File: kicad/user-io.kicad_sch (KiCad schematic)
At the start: 45 parts, among them J1 Lower Bank, J2 Upper Bank, SW1 PTS815, U1 MIMXRT1171DVMAB, U2 MAYA-W166-00B, U3 LSM6DSV, U4 LIS2MDL, U5 RTMC-G2-4IQ48, Y1 8MHz

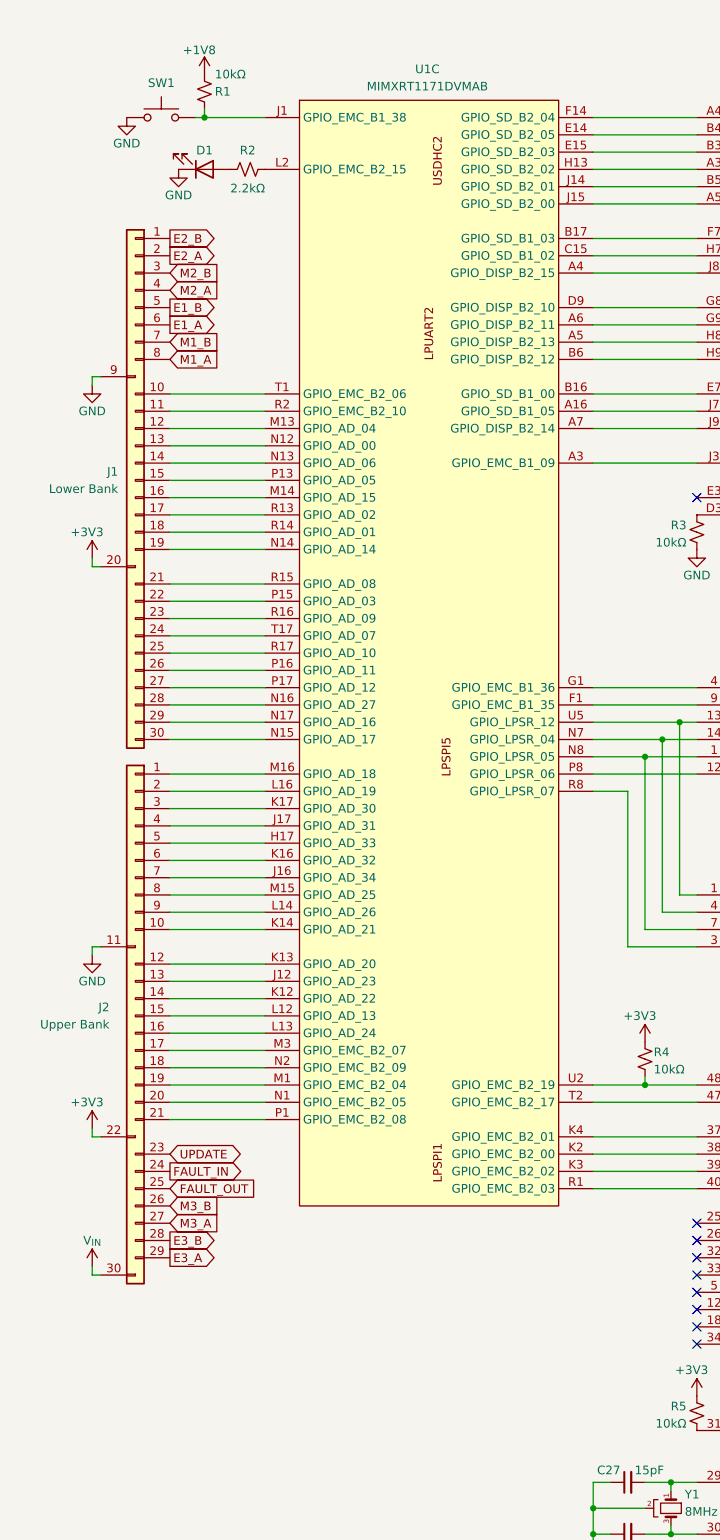
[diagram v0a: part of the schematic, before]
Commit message: moved wifi module from uSDHC2 to uSDHC1
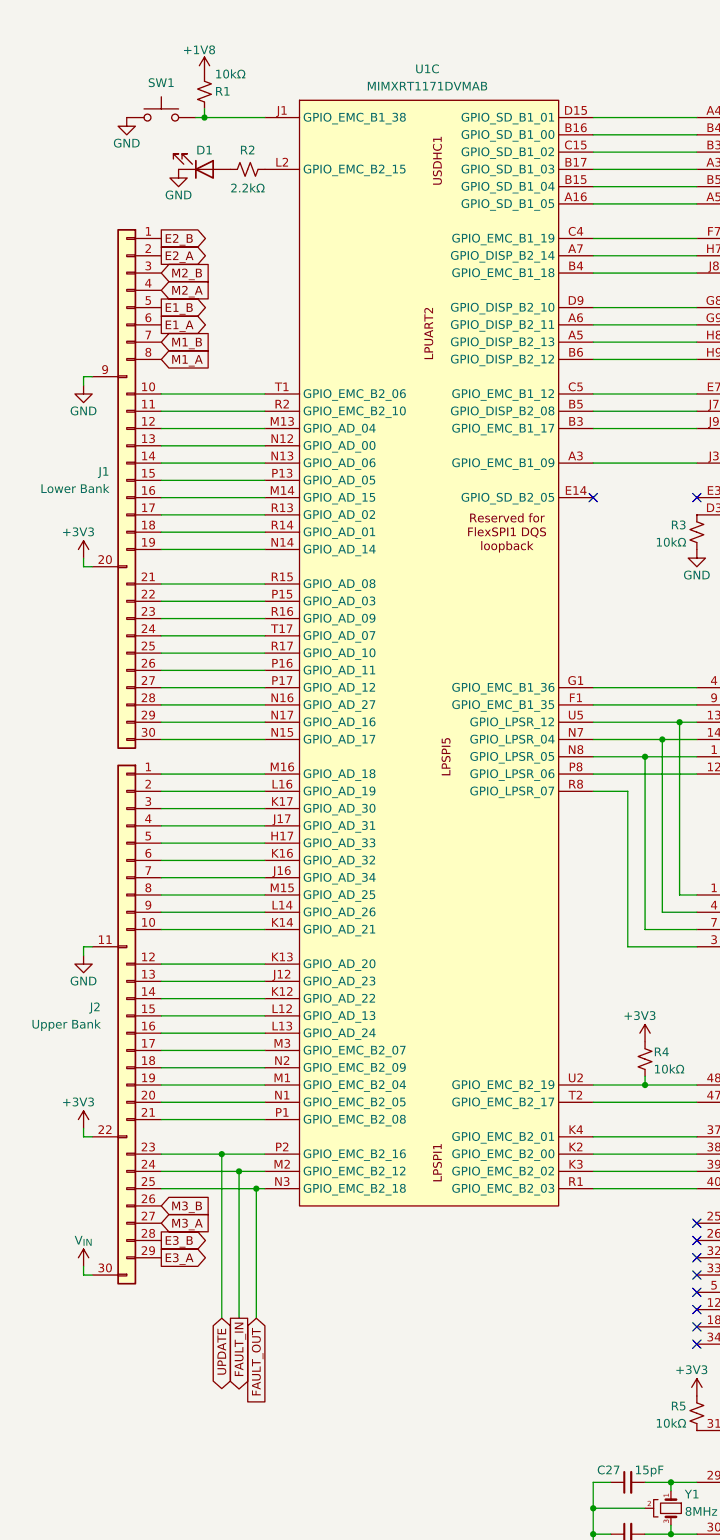
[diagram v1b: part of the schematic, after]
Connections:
- net FAULT_IN: now also U1.M2 (GPIO_EMC_B2_12)
- net FAULT_OUT: now also U1.N3 (GPIO_EMC_B2_18)
- net UPDATE: now also U1.P2 (GPIO_EMC_B2_16)
- net at U1.A16 (GPIO_SD_B1_05): now also U2.A5 (SD_DAT[3]); no longer U2.J7 (BT_RESET)
- net at U2.J8 (WLAN_DEV_WAKE): now also U1.B4 (GPIO_EMC_B1_18); no longer U1.A4 (GPIO_DISP_B2_15)
- net at U1.A7 (GPIO_DISP_B2_14): now also U2.H7 (WLAN_RESET); no longer U2.J9 (BT_DEV_WAKE)
- net at U1.B16 (GPIO_SD_B1_00): now also U2.B4 (SD_CMD); no longer U2.E7 (BT_WAKE_HOST)
- net at U1.B17 (GPIO_SD_B1_03): now also U2.A3 (SD_DAT[1]); no longer U2.F7 (WLAN_WAKE_HOST)
- net at U1.C15 (GPIO_SD_B1_02): now also U2.B3 (SD_DAT[0]); no longer U2.H7 (WLAN_RESET)
- net at U1.E14 (GPIO_SD_B2_05): no longer U2.B4 (SD_CMD)
- net at U2.A4 (SD_CLK): now also U1.D15 (GPIO_SD_B1_01); no longer U1.F14 (GPIO_SD_B2_04)
- net at U2.B5 (SD_DAT[2]): now also U1.B15 (GPIO_SD_B1_04); no longer U1.J14 (GPIO_SD_B2_01)
- new net: U1.B3 (GPIO_EMC_B1_17), U2.J9 (BT_DEV_WAKE)
- new net: U1.B5 (GPIO_DISP_B2_08), U2.J7 (BT_RESET)
- new net: U1.C4 (GPIO_EMC_B1_19), U2.F7 (WLAN_WAKE_HOST)
- new net: U1.C5 (GPIO_EMC_B1_12), U2.E7 (BT_WAKE_HOST)
- no-connect marks 11 -> 12
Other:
- moved on the sheet: J1, J2
